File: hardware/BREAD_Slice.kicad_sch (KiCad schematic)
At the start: 0 parts

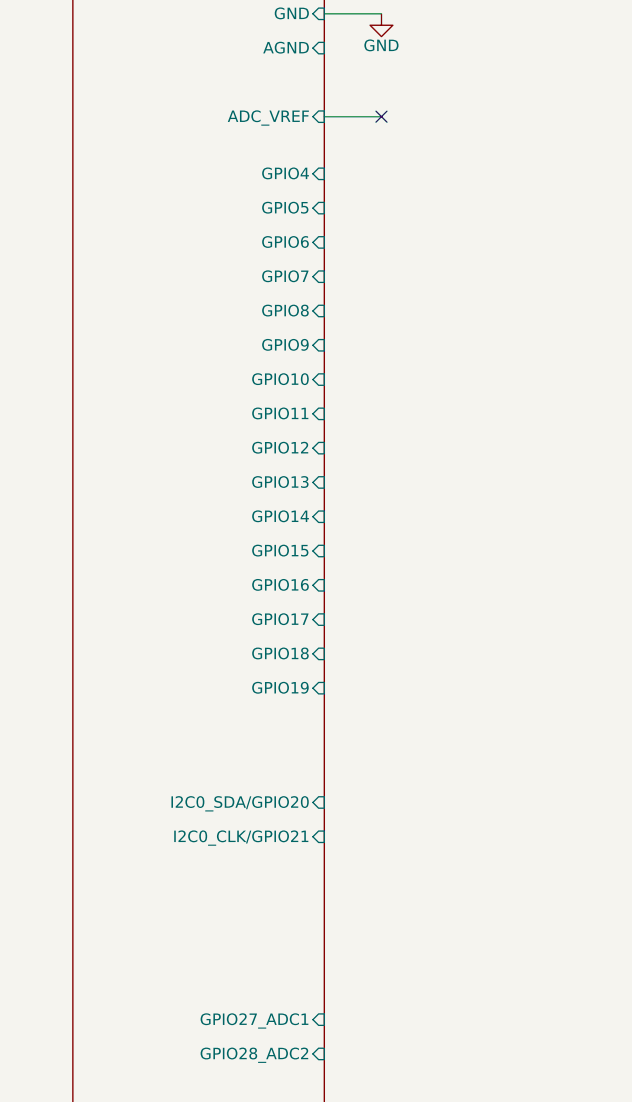
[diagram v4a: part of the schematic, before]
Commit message: added pins 2 and 3 to hierarchical sheet
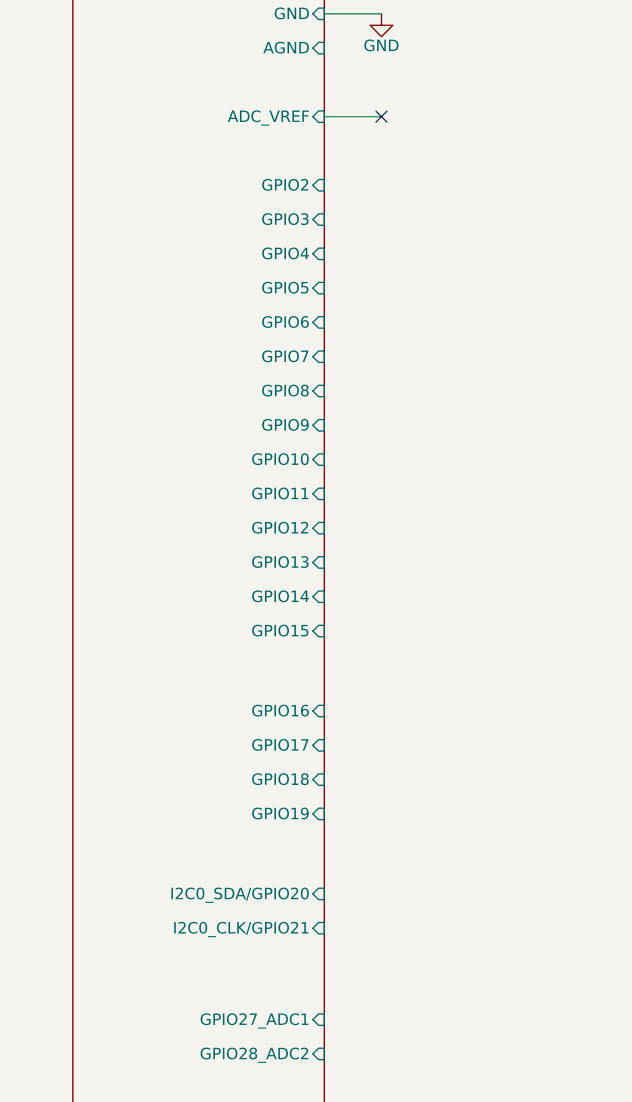
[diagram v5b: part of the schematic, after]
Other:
- sheet slice_template ports: added GPIO2, GPIO3; removed none
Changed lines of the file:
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@@
 		)
 		(pin "GPIO4" input
-			(at 45.72 78.74 0)
+			(at 45.72 87.63 0)
 			(effects
 				(font
@@
 		)
 		(pin "GPIO5" input
-			(at 45.72 82.55 0)
+			(at 45.72 91.44 0)
 			(effects
 				(font
@@
 		)
 		(pin "GPIO8" input
-			(at 45.72 93.98 0)
+			(at 45.72 102.87 0)
 			(effects
 				(font
@@
 		)
 		(pin "GPIO9" input
-			(at 45.72 97.79 0)
+			(at 45.72 106.68 0)
 			(effects
 				(font
@@
 		)
 		(pin "GPIO10" input
-			(at 45.72 101.6 0)
+			(at 45.72 110.49 0)
 			(effects
 				(font
@@
 		)
 		(pin "GPIO11" input
-			(at 45.72 105.41 0)
+			(at 45.72 114.3 0)
 			(effects
 				(font
@@
 		)
 		(pin "GPIO12" input
-			(at 45.72 109.22 0)
+			(at 45.72 118.11 0)
 			(effects
 				(font
@@
 		)
 		(pin "GPIO13" input
-			(at 45.72 113.03 0)
+			(at 45.72 121.92 0)
 			(effects
 				(font
@@
 		)
 		(pin "GPIO14" input
-			(at 45.72 116.84 0)
+			(at 45.72 125.73 0)
 			(effects
 				(font
@@
 		)
 		(pin "GPIO15" input
-			(at 45.72 120.65 0)
+			(at 45.72 129.54 0)
 			(effects
 				(font
@@
 		)
 		(pin "GPIO6" input
-			(at 45.72 86.36 0)
+			(at 45.72 95.25 0)
 			(effects
 				(font
@@
 		)
 		(pin "GPIO7" input
-			(at 45.72 90.17 0)
+			(at 45.72 99.06 0)
 			(effects
 				(font
@@
 		)
 		(pin "I2C0_CLK{slash}GPIO21" input
-			(at 45.72 152.4 0)
+			(at 45.72 162.56 0)
 			(effects
 				(font
@@
 		)
 		(pin "I2C0_SDA{slash}GPIO20" input
-			(at 45.72 148.59 0)
+			(at 45.72 158.75 0)
 			(effects
 				(font
@@
 		)
 		(pin "GPIO16" input
-			(at 45.72 124.46 0)
+			(at 45.72 138.43 0)
 			(effects
 				(font
@@
 		)
 		(pin "GPIO17" input
-			(at 45.72 128.27 0)
+			(at 45.72 142.24 0)
 			(effects
 				(font
@@
 		)
 		(pin "GPIO18" input
-			(at 45.72 132.08 0)
+			(at 45.72 146.05 0)
 			(effects
 				(font
@@
 		)
 		(pin "GPIO19" input
-			(at 45.72 135.89 0)
-			(effects
-				(font
+			(at 45.72 149.86 0)
+			(effects
+				(font
+					(size 1.27 1.27)
+				)
+				(justify right)
+			)
+		)
+		(pin "GPIO2" input
+			(at 45.72 80.01 0)
+			(effects
+				(font
+					(size 1.27 1.27)
+				)
+				(justify right)
+			)
+		)
+		(pin "GPIO3" input
+			(at 45.72 83.82 0)
+			(effects
+				(font

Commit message: fix: rewire gnd caps around pico
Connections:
- no-connect marks 3 -> 25
